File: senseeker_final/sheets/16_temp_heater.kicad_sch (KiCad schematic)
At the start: 13 parts, among them J1 2.54-1*6PHeader-RA, Q1 2N7002, Q2 CJQ4435, Q3 currentmirror, U9 ADS1115IDGSR

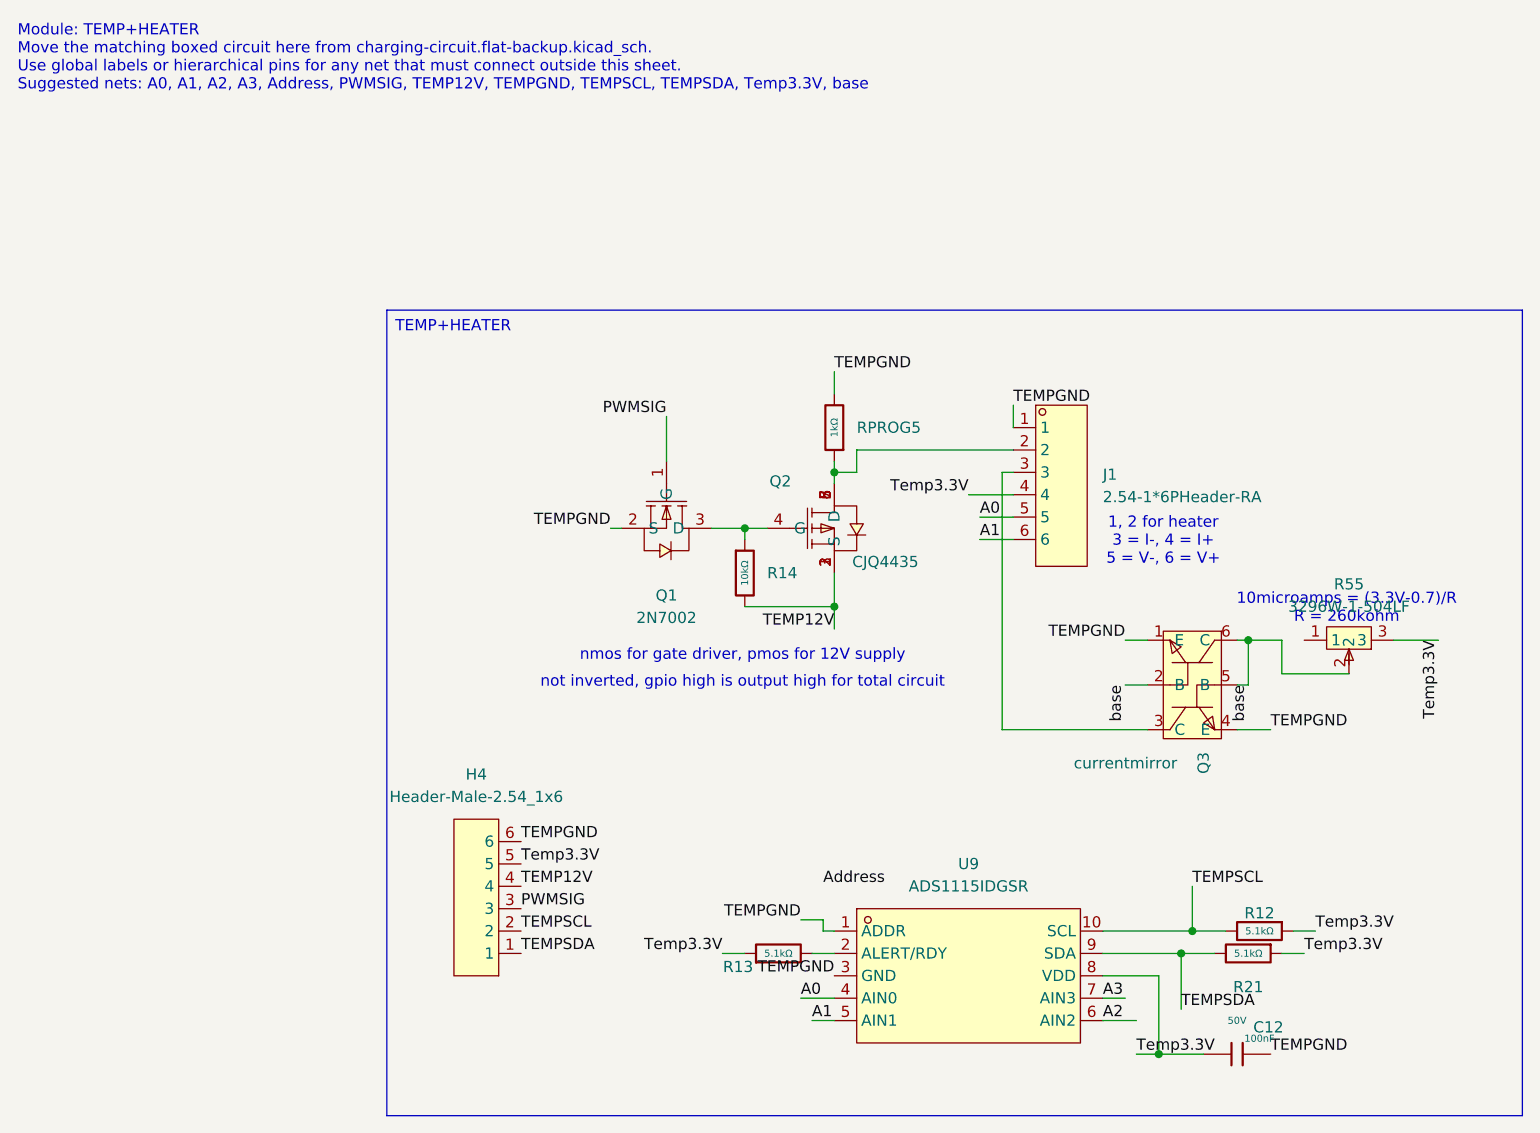
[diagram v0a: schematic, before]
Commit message: formatting changes for LM2596, now ready to branch of off and make our seperate PCB and then compare
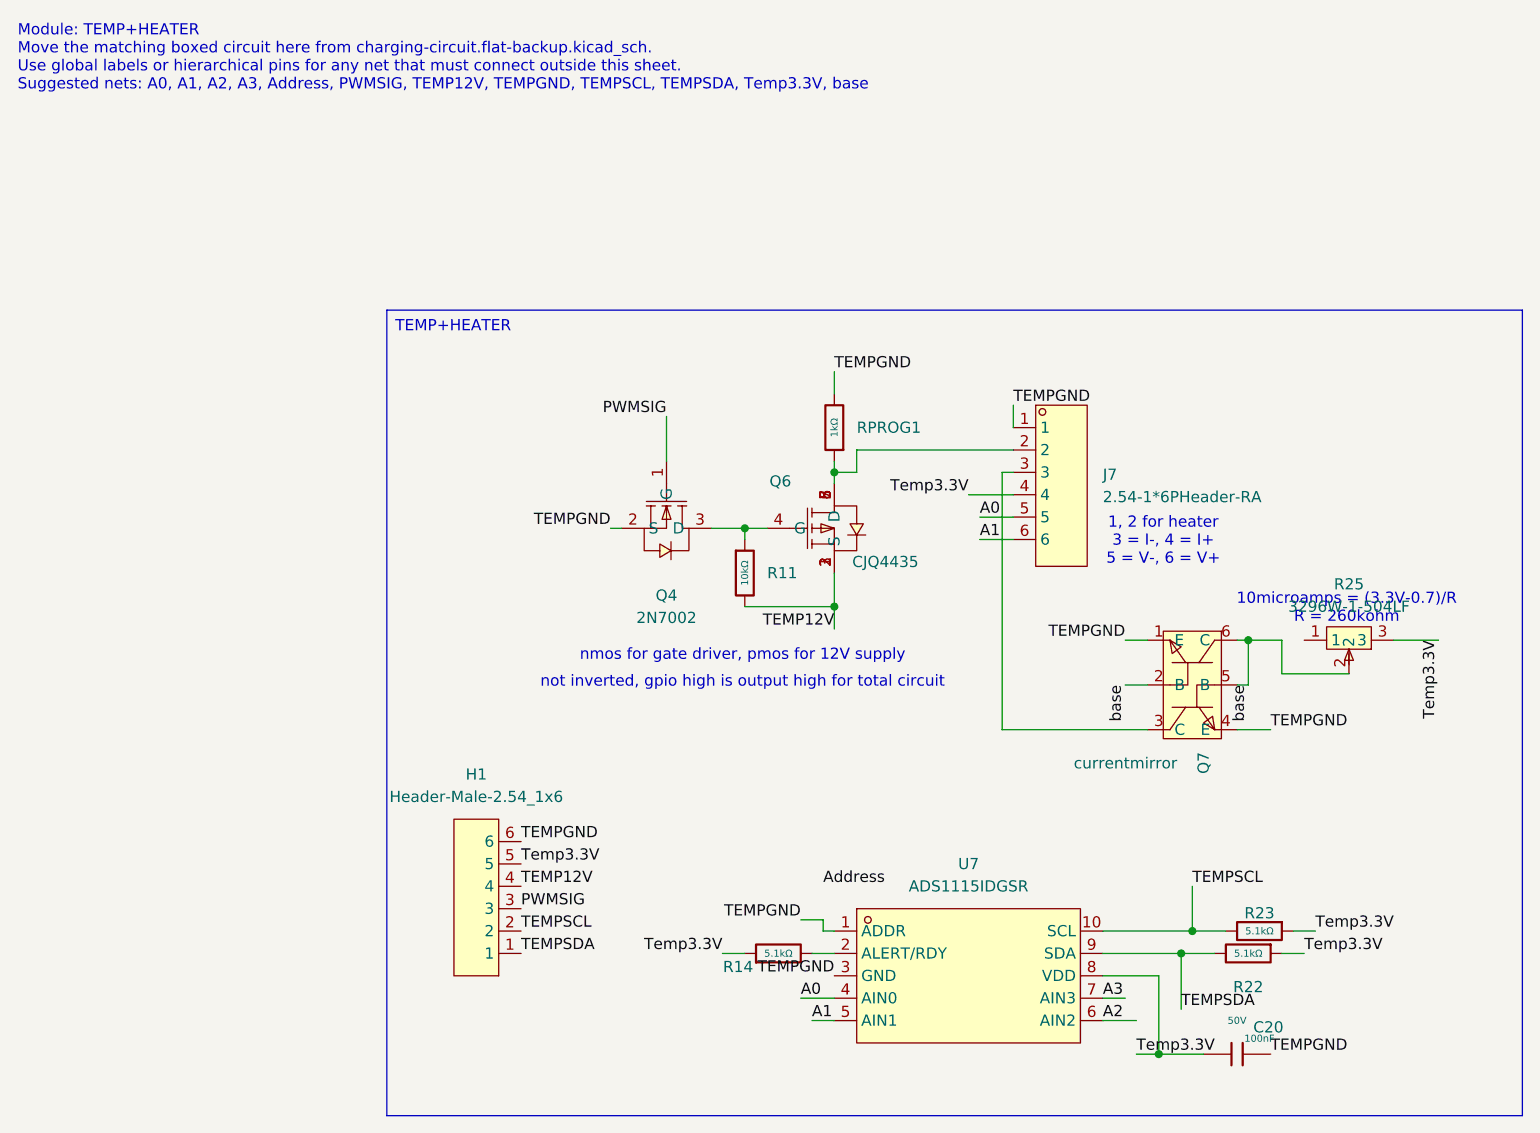
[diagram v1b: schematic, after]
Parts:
- renumbered C12 to C20, H4 to H1, J1 to J7, Q1 to Q4, Q2 to Q6, Q3 to Q7, R14 to R11, R13 to R14, R21 to R22, R12 to R23, R55 to R25, RPROG5 to RPROG1, U9 to U7
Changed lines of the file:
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@@
 		(on_board yes)
 		(dnp no)
-		(property "Reference" "R13"
+		(property "Reference" "R14"
 			(at 107.188 128.524 90)
 			(effects
@@
 			(project "senseeker_final"
 				(path "/529bc8a5-ffae-43ac-972d-caccc3afab85/c2b703a4-2e88-4383-8b77-8614951a81a3"
-					(reference "R13")
+					(reference "R14")
 					(unit 1)
 				)
@@
 		(dnp no)
 		(fields_autoplaced yes)
-		(property "Reference" "U9"
+		(property "Reference" "U7"
 			(at 133.35 116.84 0)
 			(effects
@@
 			(project "senseeker_final"
 				(path "/529bc8a5-ffae-43ac-972d-caccc3afab85/c2b703a4-2e88-4383-8b77-8614951a81a3"
-					(reference "U9")
+					(reference "U7")
 					(unit 1)
 				)
@@
 		(on_board yes)
 		(dnp no)
-		(property "Reference" "C12"
+		(property "Reference" "C20"
 			(at 167.386 135.382 90)
 			(effects
@@
 			(project "senseeker_final"
 				(path "/529bc8a5-ffae-43ac-972d-caccc3afab85/c2b703a4-2e88-4383-8b77-8614951a81a3"
-					(reference "C12")
+					(reference "C20")
 					(unit 1)
 				)
@@
 		(dnp no)
 		(fields_autoplaced yes)
-		(property "Reference" "RPROG5"
+		(property "Reference" "RPROG1"
 			(at 120.65 67.3099 0)
 			(effects
@@
 			(project "senseeker_final"
 				(path "/529bc8a5-ffae-43ac-972d-caccc3afab85/c2b703a4-2e88-4383-8b77-8614951a81a3"
-					(reference "RPROG5")
+					(reference "RPROG1")
 					(unit 1)
 				)
@@
 		(dnp no)
 		(fields_autoplaced yes)
-		(property "Reference" "Q1"
+		(property "Reference" "Q4"
 			(at 99.06 86.36 90)
 			(effects
@@
 			(project "senseeker_final"
 				(path "/529bc8a5-ffae-43ac-972d-caccc3afab85/c2b703a4-2e88-4383-8b77-8614951a81a3"
-					(reference "Q1")
+					(reference "Q4")
 					(unit 1)
 				)
@@
 		(on_board yes)
 		(dnp no)
-		(property "Reference" "R12"
+		(property "Reference" "R23"
 			(at 166.37 122.428 90)
 			(effects
@@
 			(project "senseeker_final"
 				(path "/529bc8a5-ffae-43ac-972d-caccc3afab85/c2b703a4-2e88-4383-8b77-8614951a81a3"
-					(reference "R12")
+					(reference "R23")
 					(unit 1)
 				)
@@
 		(dnp no)
 		(fields_autoplaced yes)
-		(property "Reference" "R55"
+		(property "Reference" "R25"
 			(at 176.53 85.09 90)
 			(effects
@@
 			(project "senseeker_final"
 				(path "/529bc8a5-ffae-43ac-972d-caccc3afab85/c2b703a4-2e88-4383-8b77-8614951a81a3"
-					(reference "R55")
+					(reference "R25")
 					(unit 1)
 				)
@@
 		(dnp no)
 		(fields_autoplaced yes)
-		(property "Reference" "J1"
+		(property "Reference" "J7"
 			(at 148.59 72.6449 0)
 			(effects
@@
 			(project "senseeker_final"
 				(path "/529bc8a5-ffae-43ac-972d-caccc3afab85/c2b703a4-2e88-4383-8b77-8614951a81a3"
-					(reference "J1")
+					(reference "J7")
 					(unit 1)
 				)
@@
 		(on_board yes)
 		(dnp no)
-		(property "Reference" "Q2"
+		(property "Reference" "Q6"
 			(at 110.744 73.406 0)
 			(effects
@@
 			(project "senseeker_final"
 				(path "/529bc8a5-ffae-43ac-972d-caccc3afab85/c2b703a4-2e88-4383-8b77-8614951a81a3"
-					(reference "Q2")
+					(reference "Q6")
 					(unit 1)
 				)
@@
 		(on_board yes)
 		(dnp no)
-		(property "Reference" "Q3"
+		(property "Reference" "Q7"
 			(at 160.0201 104.14 0)
 			(effects
@@
 			(project "senseeker_final"
 				(path "/529bc8a5-ffae-43ac-972d-caccc3afab85/c2b703a4-2e88-4383-8b77-8614951a81a3"
-					(reference "Q3")
+					(reference "Q7")
 					(unit 1)
 				)
@@
 		(dnp no)
 		(fields_autoplaced yes)
-		(property "Reference" "R21"
+		(property "Reference" "R22"
 			(at 165.1 130.81 90)
 			(effects
@@
 			(project "senseeker_final"
 				(path "/529bc8a5-ffae-43ac-972d-caccc3afab85/c2b703a4-2e88-4383-8b77-8614951a81a3"
-					(reference "R21")
+					(reference "R22")
 					(unit 1)
 				)
@@
 		(dnp no)
 		(fields_autoplaced yes)
-		(property "Reference" "R14"
+		(property "Reference" "R11"
 			(at 110.49 83.8199 0)
 			(effects
@@
 			(project "senseeker_final"
 				(path "/529bc8a5-ffae-43ac-972d-caccc3afab85/c2b703a4-2e88-4383-8b77-8614951a81a3"
-					(reference "R14")
+					(reference "R11")
 					(unit 1)
 				)
@@
 		(dnp no)
 		(fields_autoplaced yes)
-		(property "Reference" "H4"
+		(property "Reference" "H1"
 			(at 77.47 106.68 0)
 			(effects
@@
 			(project "senseeker_final"
 				(path "/529bc8a5-ffae-43ac-972d-caccc3afab85/c2b703a4-2e88-4383-8b77-8614951a81a3"
-					(reference "H4")
-					(unit 1)
-				)
+					(reference "H1")
+					(unit 1)
+				)
